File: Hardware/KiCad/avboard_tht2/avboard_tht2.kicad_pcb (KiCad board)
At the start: 4 copper layers, 177 x 152.1 mm, 139 parts, among them IC1 AS7C256C-15PCN, IC2_AUD0 74HC32, IC36 74HC4040, IC37 74HC30, IC39 74HC00, IC40 74HC4040, IC41 74HC00, IC43 74HC00, IC44 74HC86, IC45 74HC00, IC46 74HC257, IC47 74HC257, IC48 74HC564, IC4_AUD0 74HC00, IC53 74HC04, IC6_AUD0 74HC74, IC7_AUD0 LM358N, IC9 AS7C256C-15PCN, J1 5V, J2 5V, U1 W65C02S, U2 THS7374, U3 74VHC373, U4 74VHC373, U5 74VHC373, U8 74HC244, U9 74HC244

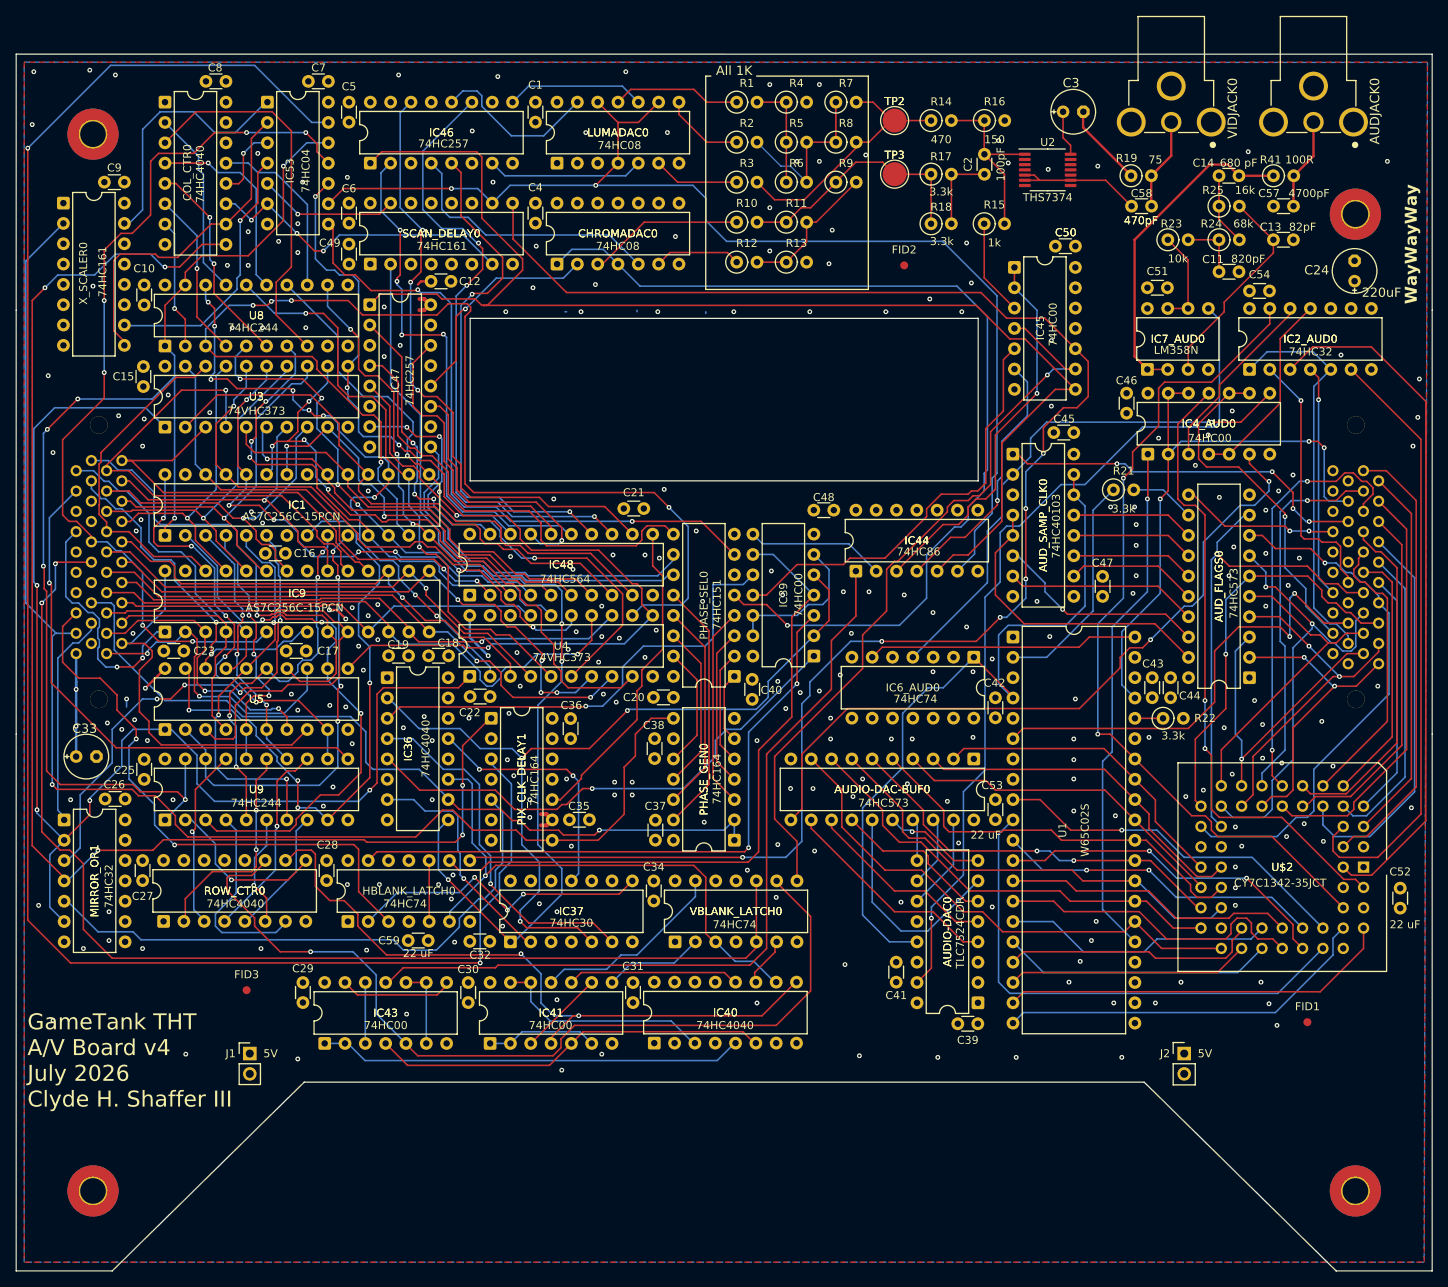
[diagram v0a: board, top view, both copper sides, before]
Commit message: add barrier between pcb edge and VCC plane
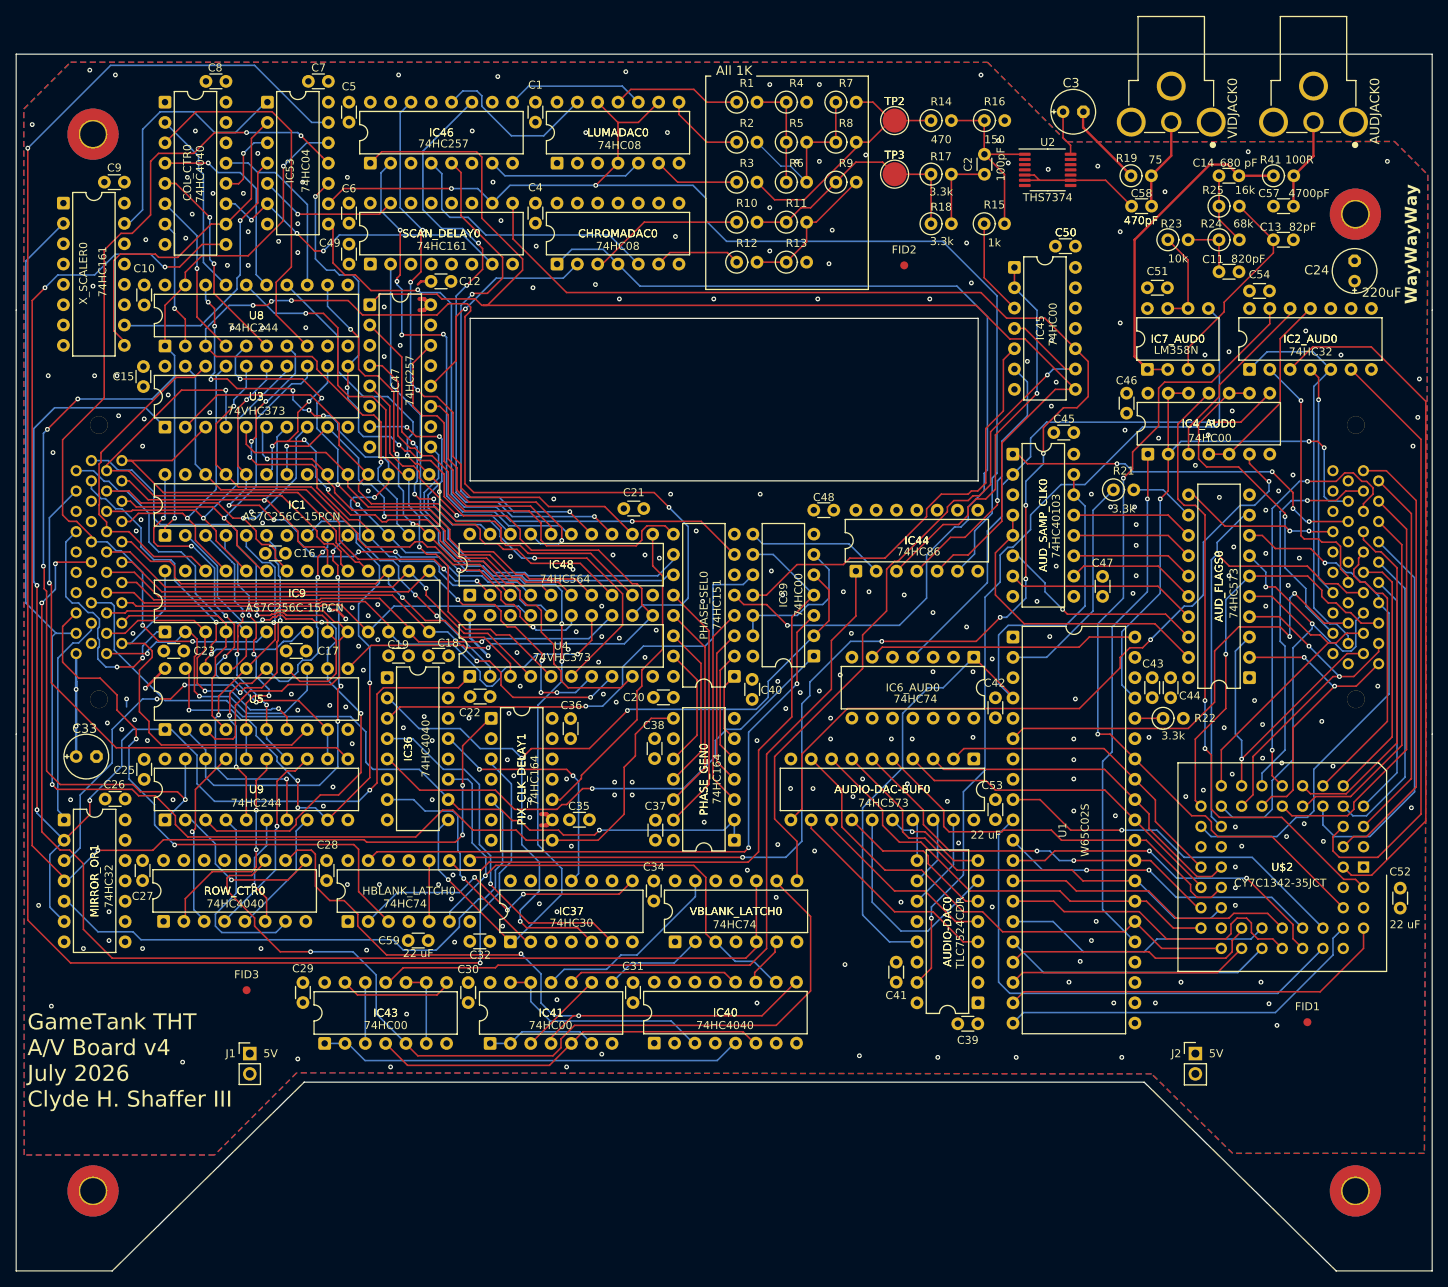
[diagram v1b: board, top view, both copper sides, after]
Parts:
- moved J2 1.40 mm to (147.4, 124.9)
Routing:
- net VCC: track 58.8 -> 57.4 mm, vias 262 -> 280
- net /Composite Video Generator/~{VWE}: track 112.3 -> 111.8 mm, vias 6 -> 4
- net Net-(AUDIO-DAC0-VREF): track 108.4 -> 107.9 mm
- net GND: vias 0 -> 1
